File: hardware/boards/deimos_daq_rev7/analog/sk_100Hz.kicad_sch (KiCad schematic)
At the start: 9 parts, among them Q15001 MMBFJ113, Q15002 MMBFJ113, U15001 OPA196xDBV

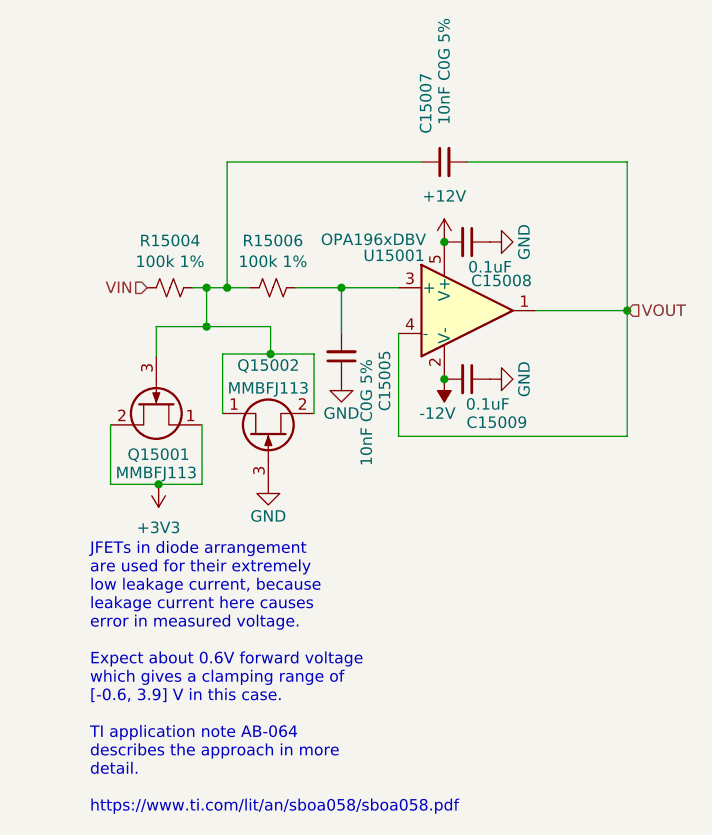
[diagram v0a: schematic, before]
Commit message: update schematic with regulated OVP rail
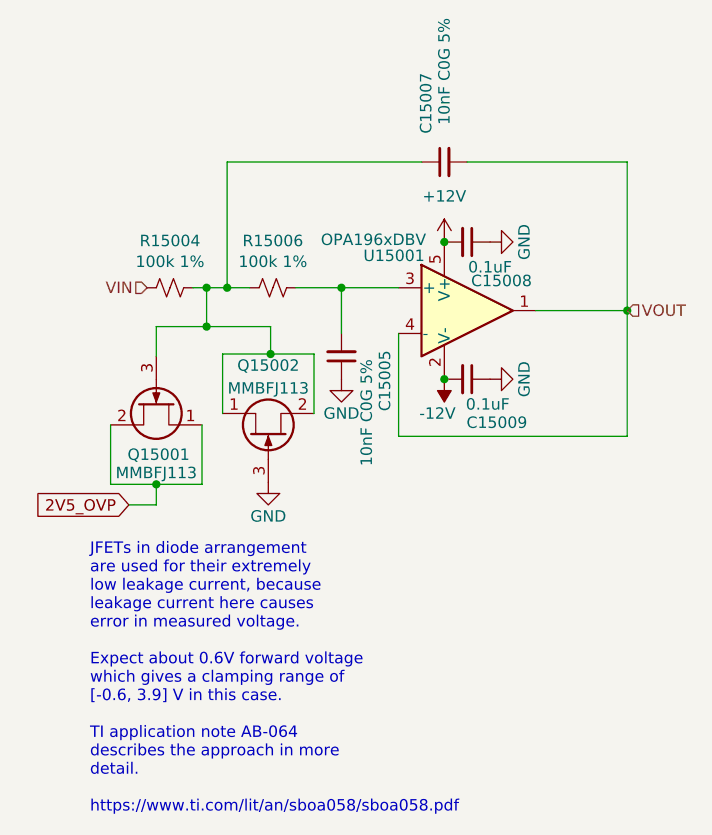
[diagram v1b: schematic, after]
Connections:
- net +3V3 renamed 2V5_OVP
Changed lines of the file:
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@@
+	)
+	(junction
+		(at 81.026 104.394)
+		(diameter 0)
+		(color 0 0 0 0)
 	)
 	(junction
@@
 	)
 	(junction
-		(at 81.28 104.394)
-		(diameter 0)
-		(color 0 0 0 0)
-	)
-	(junction
 		(at 86.614 82.55)
 		(diameter 0)
@@
 	(wire
 		(pts
-			(xy 75.946 104.394) (xy 81.28 104.394)
+			(xy 75.946 104.394) (xy 81.026 104.394)
 		)
 		(stroke
@@
 	(wire
 		(pts
-			(xy 81.28 104.394) (xy 86.106 104.394)
-		)
-		(stroke
-			(width 0)
-			(type default)
-		)
-	)
-	(wire
-		(pts
 			(xy 88.392 89.916) (xy 93.726 89.916)
 		)
@@
 	(wire
 		(pts
+			(xy 81.026 106.68) (xy 81.026 104.394)
+		)
+		(stroke
+			(width 0)
+			(type default)
+		)
+	)
+	(wire
+		(pts
 			(xy 133.35 68.58) (xy 133.35 85.09)
 		)
@@
 		(pts
 			(xy 86.614 82.55) (xy 88.9 82.55)
+		)
+		(stroke
+			(width 0)
+			(type default)
+		)
+	)
+	(wire
+		(pts
+			(xy 77.978 106.68) (xy 81.026 106.68)
+		)
+		(stroke
+			(width 0)
+			(type default)
+		)
+	)
+	(wire
+		(pts
+			(xy 81.026 104.394) (xy 86.106 104.394)
 		)
 		(stroke
@@
 			)
 			(justify left)
+		)
+	)
+	(global_label "2V5_OVP"
+		(shape input)
+		(at 77.978 106.68 180)
+		(fields_autoplaced yes)
+		(effects
+			(font
+				(size 1.27 1.27)
+			)
+			(justify right)
+		)
+		(property "Intersheetrefs" "${INTERSHEET_REFS}"
+			(at 66.8285 106.68 0)
+			(effects
+				(font
+					(size 1.27 1.27)
+				)
+				(justify right)
+				(hide yes)
+			)
 		)
 	)
@@
 					(unit 1)
 				)
-			)
-		)
-	)
-	(symbol
-		(lib_id "power:+3V3")
-		(at 81.28 104.394 180)
-		(unit 1)
-		(exclude_from_sim no)
-		(in_bom yes)
-		(on_board yes)
-		(dnp no)
-		(fields_autoplaced yes)
-		(property "Reference" "#PWR180"
-			(at 81.28 100.584 0)
-			(effects
-				(font
-					(size 1.27 1.27)
-				)
-				(hide yes)
-			)
-		)
-		(property "Value" "+3V3"
-			(at 81.28 109.22 0)
-			(effects
-				(font
-					(size 1.27 1.27)
-				)
-			)
-		)
-		(property "Footprint" ""
-			(at 81.28 104.394 0)
-			(effects
-				(font
-					(size 1.27 1.27)
-				)
-				(hide yes)
-			)
-		)
-		(property "Datasheet" ""
-			(at 81.28 104.394 0)
-			(effects
-				(font
-					(size 1.27 1.27)
-				)
-				(hide yes)
-			)
-		)
-		(property "Description" "Power symbol creates a global label with name \"+3V3\""
-			(at 81.28 104.394 0)
-			(effects
-				(font
-					(size 1.27 1.27)
-				)
-				(hide yes)
-			)
-		)
-		(pin "1"
-		)
-		(instances
-			(project "analog_i"
-				(path "/5a60c4b1-b6cb-416e-8883-8291fa089b87/c2baf18d-2b19-4edb-98b3-535275ee271f/f31a785a-aa18-4b99-9461-7c34b37be0d7"
-					(reference "#PWR180")
-					(unit 1)
-				)
-				(path "/5a60c4b1-b6cb-416e-8883-8291fa089b87/c2baf18d-2b19-4edb-98b3-535275ee271f/ed60502d-2e6d-4293-85f2-5e967a3c42d8/63cb4c21-96ec-4930-8398-5e4d00a3dfaf"
-					(reference "#PWR318")
-					(unit 1)
-				)
-			)
-			(project ""
-				(path "/c241d083-1323-4b4a-a540-956d0afb7b72/f31a785a-aa18-4b99-9461-7c34b37be0d7"
-					(reference "#PWR20005")
-					(unit 1)
-				)
-				(path "/c241d083-1323-4b4a-a540-956d0afb7b72/ed60502d-2e6d-4293-85f2-5e967a3c42d8/63cb4c21-96ec-4930-8398-5e4d00a3dfaf"
-					(reference "#PWR14005")
-					(unit 1)
-				)

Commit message: update notes for clamp voltage
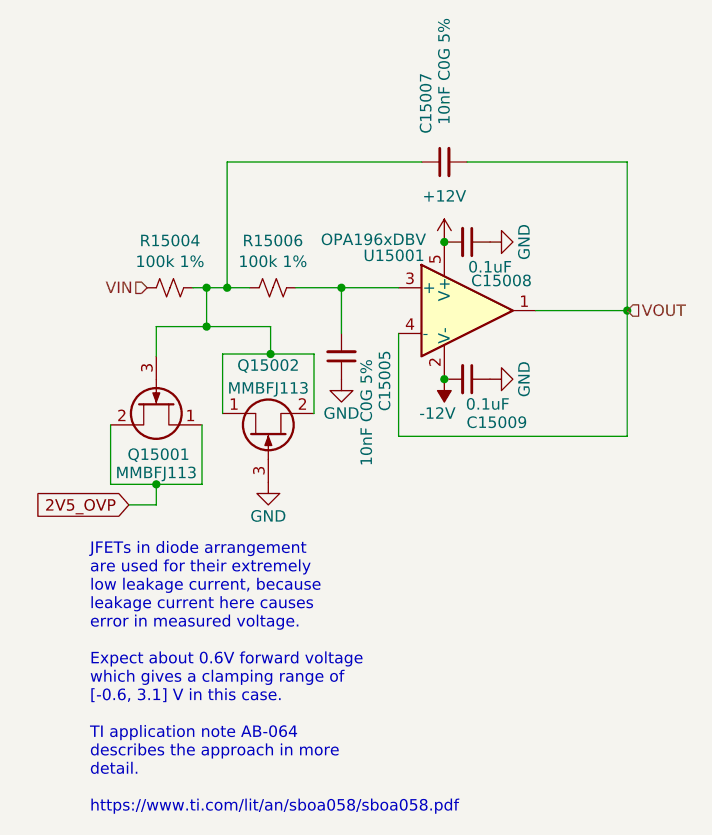
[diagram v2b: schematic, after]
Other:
- note added: "JFETs in diode arrangement are used for their extremely low leakage current, because leakage current here causes error in measured voltage. Expect about 0.6V forward voltage which gives a clamping range of [-0.6, 3.1] V in this case. TI application note AB-064 describes the approach in more detail. https://www.ti.com/lit/an/sboa058/sboa058.pdf"
- note removed: "JFETs in diode arrangement are used for their extremely low leakage current, because leakage current here causes error in measured voltage. Expect about 0.6V forward voltage which gives a clamping range of [-0.6, 3.9] V in this case. TI application note AB-064 describes the approach in more detail. https://www.ti.com/lit/an/sboa058/sboa058.pdf"
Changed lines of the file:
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@@
 		)
 	)
-	(text "JFETs in diode arrangement\nare used for their extremely\nlow leakage current, because\nleakage current here causes\nerror in measured voltage.\n\nExpect about 0.6V forward voltage\nwhich gives a clamping range of\n[-0.6, 3.9] V in this case.\n\nTI application note AB-064\ndescribes the approach in more\ndetail.\n\nhttps://www.ti.com/lit/an/sboa058/sboa058.pdf"
+	(text "JFETs in diode arrangement\nare used for their extremely\nlow leakage current, because\nleakage current here causes\nerror in measured voltage.\n\nExpect about 0.6V forward voltage\nwhich gives a clamping range of\n[-0.6, 3.1] V in this case.\n\nTI application note AB-064\ndescribes the approach in more\ndetail.\n\nhttps://www.ti.com/lit/an/sboa058/sboa058.pdf"
 		(exclude_from_sim no)
 		(at 73.66 125.984 0)
